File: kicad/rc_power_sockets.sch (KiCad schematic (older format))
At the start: 23 parts, among them IC1 ATTINY85, J1 PIR, J2 433MHZ, J3 433MHZ, P1 ICSP, P2 POWER_IN, Q1 NMOS, Q2 PMOS, U1 MCP1700T

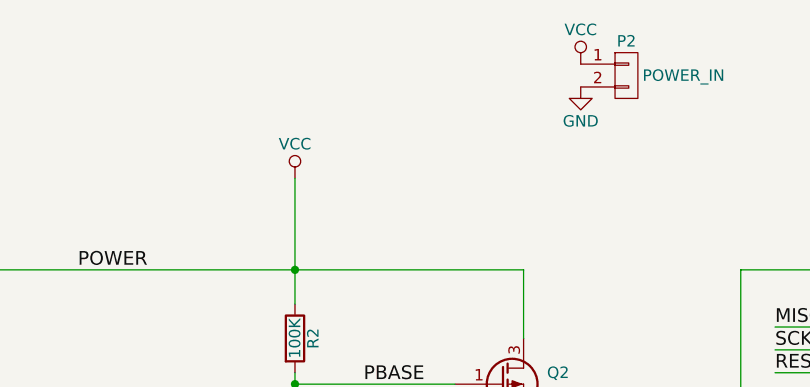
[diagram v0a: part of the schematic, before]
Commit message: Reversed polarity protection
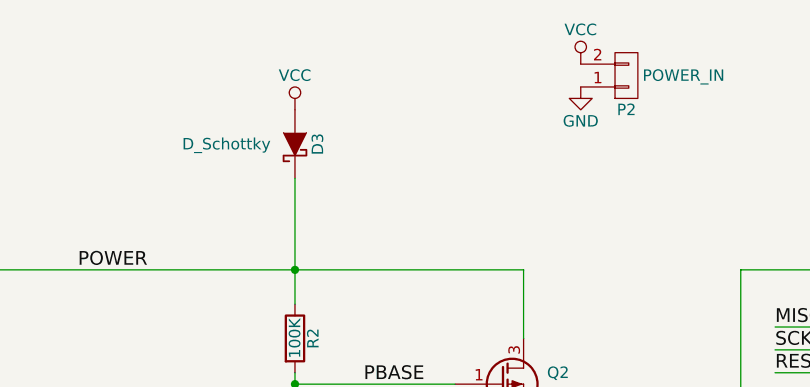
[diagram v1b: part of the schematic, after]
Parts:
- added D3: D_Schottky, Diodes_SMD:SOD-123, symbol D_Schottky
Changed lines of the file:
@@
 L VCC #PWR09
 U 1 1 56E80BFE
-P 5550 1550
-F 0 "#PWR09" H 5550 1400 50  0001 C CNN
-F 1 "VCC" H 5550 1700 50  0000 C CNN
-F 2 "" H 5550 1550 50  0000 C CNN
-F 3 "" H 5550 1550 50  0000 C CNN
-	1    5550 1550
+P 5550 1250
+F 0 "#PWR09" H 5550 1100 50  0001 C CNN
+F 1 "VCC" H 5550 1400 50  0000 C CNN
+F 2 "" H 5550 1250 50  0000 C CNN
+F 3 "" H 5550 1250 50  0000 C CNN
+	1    5550 1250
 	1    0    0    -1
 $EndComp
@@
 F 0 "U1" H 7500 3600 50  0000 C CNN
 F 1 "MCP1700T" H 7350 4100 50  0000 C CNN
-F 2 "TO_SOT_Packages_SMD:SOT-23_Handsoldering" H 7350 4000 50  0000 C CIN
+F 2 "TO_SOT_Packages_SMD:SOT-23_Handsoldering" H 7350 4000 50  0001 C CIN
 F 3 "" H 7350 3900 50  0000 C CNN
 	1    7350 3900
@@
 F 3 "" H 7000 1100 50  0000 C CNN
 	1    7000 1100
-	1    0    0    -1
+	1    0    0    1
 $EndComp
 $Comp
@@
 	0    1    1    0
 $EndComp
+$Comp
+L D_Schottky D3
+U 1 1 56F2954C
+P 5550 1400
+F 0 "D3" H 5550 1300 50  0000 C CNN
+F 1 "D_Schottky" V 5550 1700 50  0000 C CNN
+F 2 "Diodes_SMD:SOD-123" H 5550 1400 50  0001 C CNN
+F 3 "" H 5550 1400 50  0000 C CNN
+	1    5550 1400
+	0    -1   -1   0
+$EndComp
 $EndSCHEMATC

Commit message: Changed voltage regulator cap values
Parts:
- C1, C2: value 10uf -> 1uF
- C3: value 0.1uf -> 0.1uF
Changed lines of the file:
@@
 P 8000 4000
 F 0 "C2" H 8025 4100 50  0000 L CNN
-F 1 "10uf" H 8025 3900 50  0000 L CNN
+F 1 "1uF" H 8025 3900 50  0000 L CNN
 F 2 "Capacitors_SMD:C_0805_HandSoldering" H 8038 3850 50  0001 C CNN
 F 3 "" H 8000 4000 50  0000 C CNN
@@
 P 6700 4000
 F 0 "C1" H 6725 4100 50  0000 L CNN
-F 1 "10uf" H 6725 3900 50  0000 L CNN
+F 1 "1uF" H 6725 3900 50  0000 L CNN
 F 2 "Capacitors_SMD:C_0805_HandSoldering" H 6738 3850 50  0001 C CNN
 F 3 "" H 6700 4000 50  0000 C CNN
@@
 P 8250 5350
 F 0 "C3" H 8275 5450 50  0000 L CNN
-F 1 "0.1uf" H 8275 5250 50  0000 L CNN
+F 1 "0.1uF" H 8275 5250 50  0000 L CNN
 F 2 "Capacitors_SMD:C_0805_HandSoldering" H 8288 5200 50  0001 C CNN
 F 3 "" H 8250 5350 50  0000 C CNN

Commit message: Changed voltage regulator to handle higher input
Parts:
- removed U1: MCP1700T, TO_SOT_Packages_SMD:SOT-23_Handsoldering, symbol APE8865N-12-HF-3
- added U?: NCP4624DSN33T1G, SOT-23-5, symbol TLV70012DDC
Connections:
- wire segments 48 -> 49
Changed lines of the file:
@@
-$EndComp
-$Comp
-L APE8865N-12-HF-3 U1
-U 1 1 56E81B2E
-P 7350 3900
-F 0 "U1" H 7500 3600 50  0000 C CNN
-F 1 "MCP1700T" H 7350 4100 50  0000 C CNN
-F 2 "TO_SOT_Packages_SMD:SOT-23_Handsoldering" H 7350 4000 50  0001 C CIN
-F 3 "" H 7350 3900 50  0000 C CNN
-	1    7350 3900
-	1    0    0    -1
 $EndComp
 $Comp
@@
 	0    -1   -1   0
 $EndComp
+$Comp
+L TLV70012DDC U?
+U 1 1 56F2FC5E
+P 7350 3900
+F 0 "U?" H 7100 4100 50  0000 C CNN
+F 1 "NCP4624DSN33T1G" H 7350 4100 50  0000 C CNN
+F 2 "SOT-23-5" H 7350 4000 50  0000 C CIN
+F 3 "" H 7350 3900 50  0000 C CNN
+	1    7350 3900
+	1    0    0    -1
+$EndComp
+Wire Wire Line
+	6900 3850 6900 4000
 $EndSCHEMATC

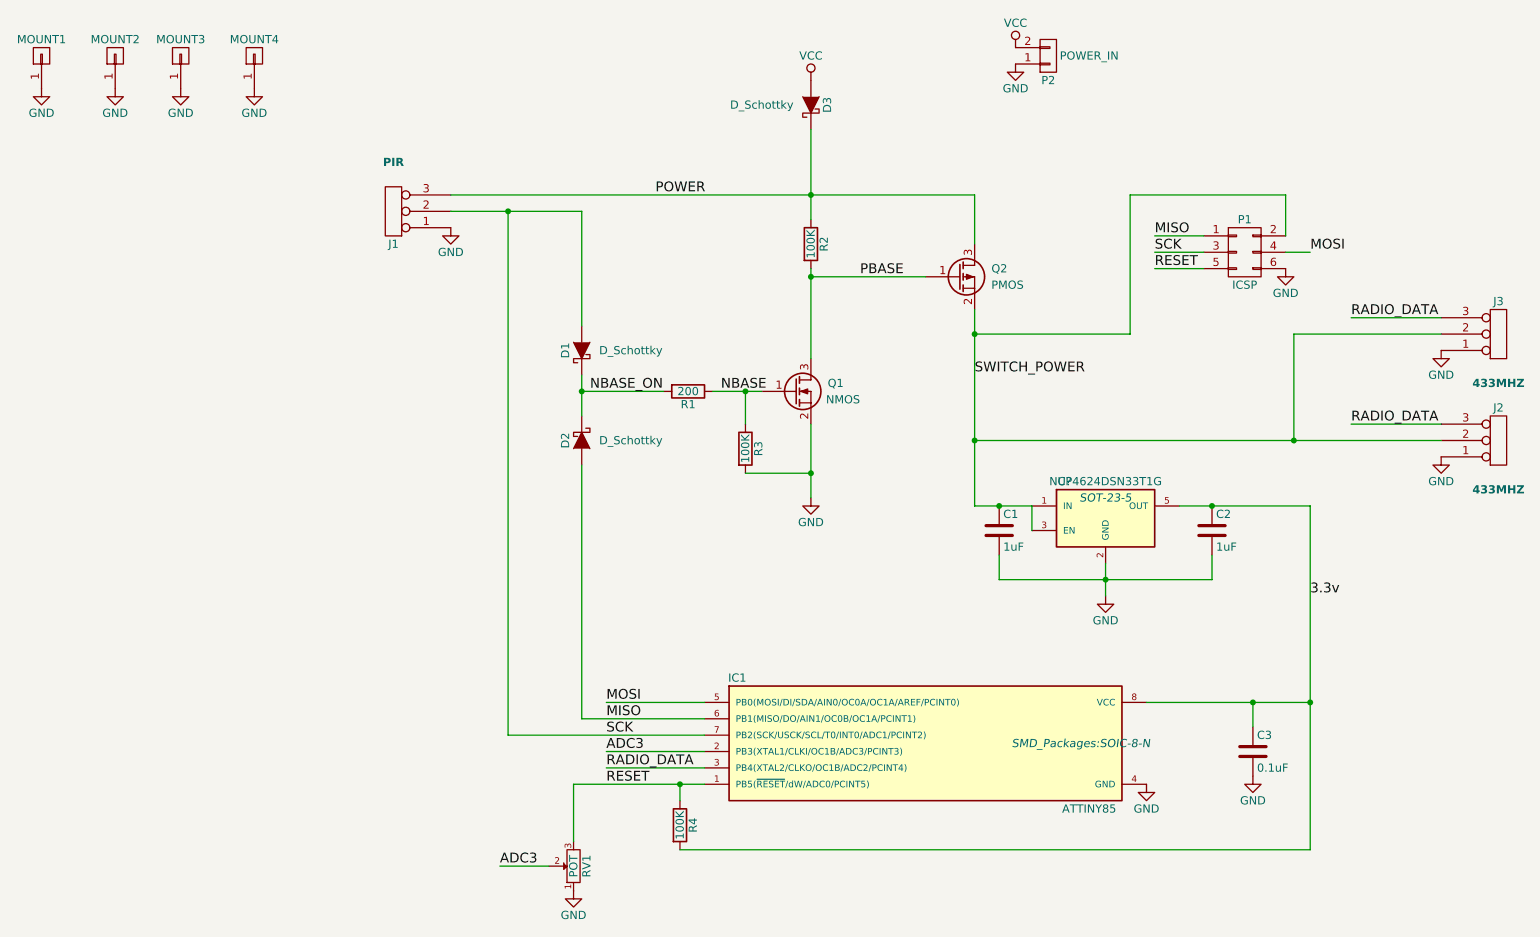
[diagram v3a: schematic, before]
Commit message: Redesign with CR2032
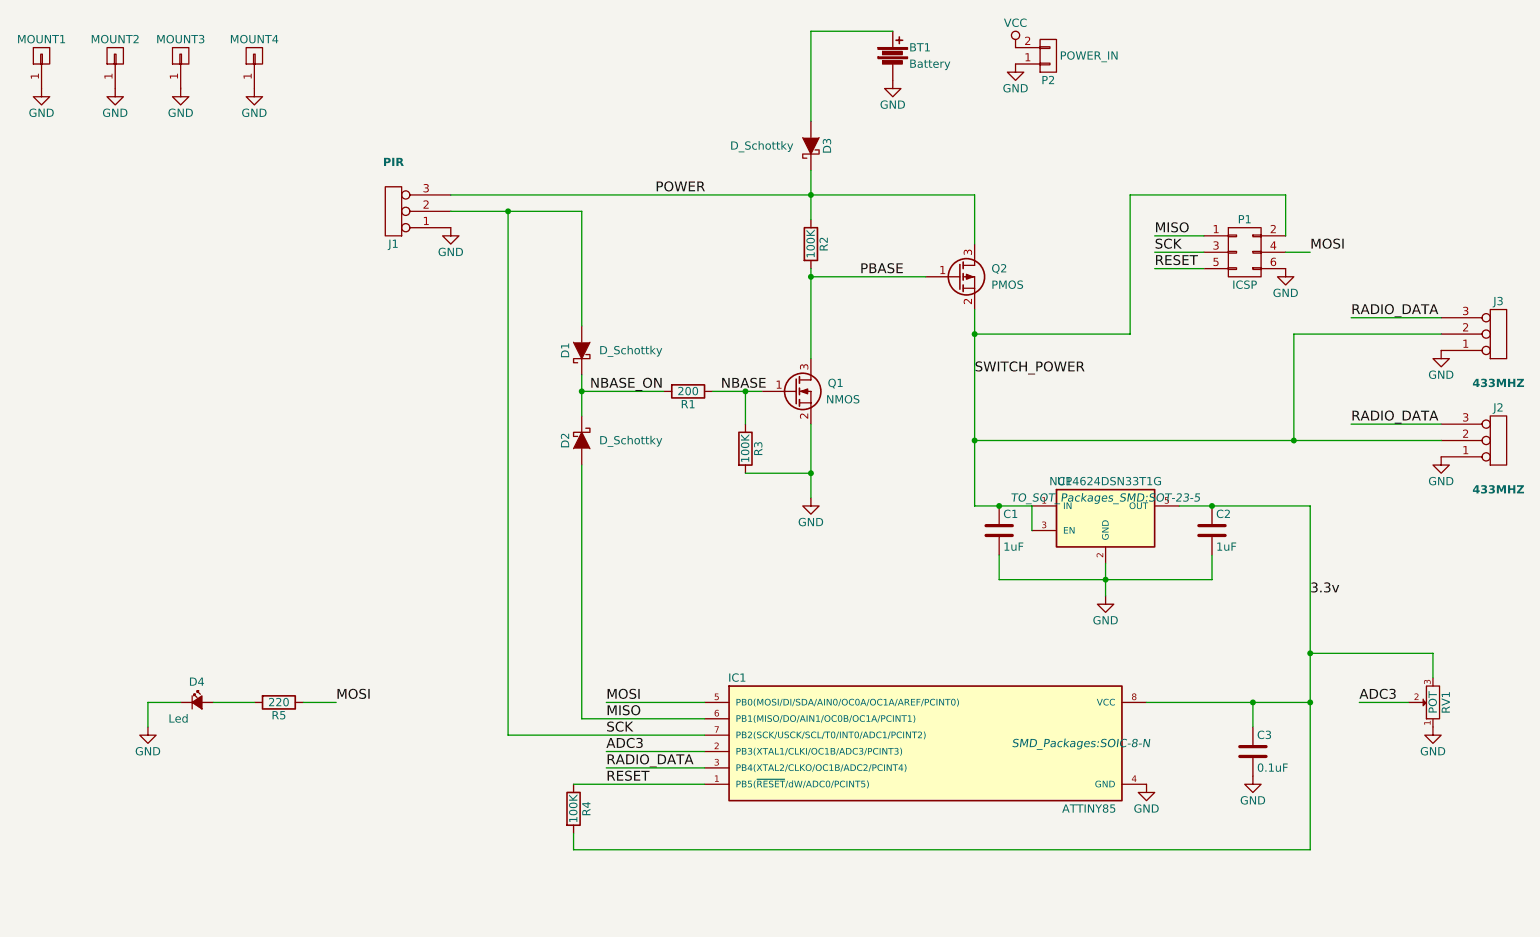
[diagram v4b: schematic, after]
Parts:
- added BT1: Battery, Connect:CR2032H, symbol Battery
- added D4: Led, LEDs:LED_0805, symbol Led_Small
- added R5: 220, Resistors_SMD:R_0805_HandSoldering, symbol R
- U1: renamed from U?; footprint SOT-23-5 -> TO_SOT_Packages_SMD:SOT-23-5
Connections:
- net 3.3v: now also RV1.3
- net GND: now also BT1.2, D4.1 (K)
- net MOSI: now also R5.1
- net RESET: no longer RV1.3
- net VCC: no longer D3.2 (A)
- new net: BT1.1, D3.2 (A)
- new net: D4.2 (A), R5.2
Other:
- moved on the sheet: D3, R4, RV1
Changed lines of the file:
@@
 L R R4
 U 1 1 56D85890
-P 4750 5800
-F 0 "R4" V 4830 5800 50  0000 C CNN
-F 1 "100K" V 4750 5800 50  0000 C CNN
-F 2 "Resistors_SMD:R_0805_HandSoldering" V 4680 5800 50  0001 C CNN
-F 3 "" H 4750 5800 50  0000 C CNN
-	1    4750 5800
+P 4100 5700
+F 0 "R4" V 4180 5700 50  0000 C CNN
+F 1 "100K" V 4100 5700 50  0000 C CNN
+F 2 "Resistors_SMD:R_0805_HandSoldering" V 4030 5700 50  0001 C CNN
+F 3 "" H 4100 5700 50  0000 C CNN
+	1    4100 5700
 	1    0    0    -1
 $EndComp
@@
 L POT-RESCUE-rc_power_sockets RV1
 U 1 1 56E809B9
-P 4100 6050
-F 0 "RV1" H 4100 5970 50  0000 C CNN
-F 1 "POT" H 4100 6050 50  0000 C CNN
-F 2 "Potentiometers:Potentiometer_WirePads_Small" H 4100 6050 50  0001 C CNN
-F 3 "" H 4100 6050 50  0000 C CNN
-	1    4100 6050
+P 9350 5050
+F 0 "RV1" H 9350 4970 50  0000 C CNN
+F 1 "POT" H 9350 5050 50  0000 C CNN
+F 2 "Potentiometers:Potentiometer_WirePads_Small" H 9350 5050 50  0001 C CNN
+F 3 "" H 9350 5050 50  0000 C CNN
+	1    9350 5050
 	0    -1   -1   0
 $EndComp
@@
 L GND #PWR08
 U 1 1 56E80AFC
-P 4100 6200
-F 0 "#PWR08" H 4100 5950 50  0001 C CNN
-F 1 "GND" H 4100 6050 50  0000 C CNN
-F 2 "" H 4100 6200 50  0000 C CNN
-F 3 "" H 4100 6200 50  0000 C CNN
-	1    4100 6200
-	1    0    0    -1
-$EndComp
-$Comp
-L VCC #PWR09
-U 1 1 56E80BFE
-P 5550 1250
-F 0 "#PWR09" H 5550 1100 50  0001 C CNN
-F 1 "VCC" H 5550 1400 50  0000 C CNN
-F 2 "" H 5550 1250 50  0000 C CNN
-F 3 "" H 5550 1250 50  0000 C CNN
-	1    5550 1250
+P 9350 5200
+F 0 "#PWR08" H 9350 4950 50  0001 C CNN
+F 1 "GND" H 9350 5050 50  0000 C CNN
+F 2 "" H 9350 5200 50  0000 C CNN
+F 3 "" H 9350 5200 50  0000 C CNN
+	1    9350 5200
 	1    0    0    -1
 $EndComp
 Text Label 4300 5350 0    60   ~ 0
 ADC3
-Text Label 3650 6050 0    60   ~ 0
+Text Label 8900 5050 0    60   ~ 0
 ADC3
 $Comp
@@
 NBASE
 $Comp
-L GND #PWR010
+L GND #PWR09
 U 1 1 56EEF4F7
 P 6800 1150
-F 0 "#PWR010" H 6800 900 50  0001 C CNN
+F 0 "#PWR09" H 6800 900 50  0001 C CNN
 F 1 "GND" H 6800 1000 50  0000 C CNN
 F 2 "" H 6800 1150 50  0000 C CNN
@@
 RADIO_DATA
 $Comp
-L GND #PWR011
+L GND #PWR010
 U 1 1 56EEFB0C
 P 9400 2900
-F 0 "#PWR011" H 9400 2650 50  0001 C CNN
+F 0 "#PWR010" H 9400 2650 50  0001 C CNN
 F 1 "GND" H 9400 2750 50  0000 C CNN
 F 2 "" H 9400 2900 50  0000 C CNN
@@
 	4900 5050 4300 5050
 Wire Wire Line
-	4100 5550 4900 5550
-Wire Wire Line
 	4900 5450 4300 5450
 Wire Wire Line
@@
 	3700 5250 4900 5250
 Wire Wire Line
-	5550 1550 5550 2100
+	5550 1800 5550 2100
 Wire Wire Line
 	5550 3350 5550 3800
@@
 Connection ~ 5150 3150
 Wire Wire Line
-	4750 5650 4750 5550
-Connection ~ 4750 5550
-Wire Wire Line
-	8600 5950 4750 5950
+	8600 5950 4100 5950
 Connection ~ 8600 5050
 Wire Wire Line
@@
 Connection ~ 8250 5050
 Wire Wire Line
-	3950 6050 3650 6050
+	9200 5050 8900 5050
 Wire Wire Line
 	4900 5350 4300 5350
@@
 Wire Wire Line
 	7600 5050 8600 5050
-Wire Wire Line
-	4100 5550 4100 5900
 Wire Wire Line
 	8450 2200 8450 1950
@@
 $EndComp
 $Comp
-L GND #PWR012
+L GND #PWR011
 U 1 1 56F02CD0
 P 1700 1300
-F 0 "#PWR012" H 1700 1050 50  0001 C CNN
+F 0 "#PWR011" H 1700 1050 50  0001 C CNN
 F 1 "GND" H 1700 1150 50  0000 C CNN
 F 2 "" H 1700 1300 50  0000 C CNN
@@
 $EndComp
 $Comp
-L GND #PWR013
+L GND #PWR012
 U 1 1 56F02EF0
 P 2150 1300
-F 0 "#PWR013" H 2150 1050 50  0001 C CNN
+F 0 "#PWR012" H 2150 1050 50  0001 C CNN
 F 1 "GND" H 2150 1150 50  0000 C CNN
 F 2 "" H 2150 1300 50  0000 C CNN
@@
 $EndComp
 $Comp
-L GND #PWR014
+L GND #PWR013
 U 1 1 56F02F76
 P 850 1300
-F 0 "#PWR014" H 850 1050 50  0001 C CNN
+F 0 "#PWR013" H 850 1050 50  0001 C CNN
 F 1 "GND" H 850 1150 50  0000 C CNN
 F 2 "" H 850 1300 50  0000 C CNN
@@
 $EndComp
 $Comp
-L GND #PWR015
+L GND #PWR014
 U 1 1 56F02F82
 P 1300 1300
-F 0 "#PWR015" H 1300 1050 50  0001 C CNN
+F 0 "#PWR014" H 1300 1050 50  0001 C CNN
 F 1 "GND" H 1300 1150 50  0000 C CNN
 F 2 "" H 1300 1300 50  0000 C CNN
@@
 $EndComp
 $Comp
-L VCC #PWR016
+L VCC #PWR015
 U 1 1 56F0619B
 P 6800 1050
-F 0 "#PWR016" H 6800 900 50  0001 C CNN
+F 0 "#PWR015" H 6800 900 50  0001 C CNN
 F 1 "VCC" H 6800 1200 50  0000 C CNN
 F 2 "" H 6800 1050 50  0000 C CNN
@@
 L D_Schottky D3
 U 1 1 56F2954C
-P 5550 1400
-F 0 "D3" H 5550 1300 50  0000 C CNN
-F 1 "D_Schottky" V 5550 1700 50  0000 C CNN
-F 2 "Diodes_SMD:SOD-123" H 5550 1400 50  0001 C CNN
-F 3 "" H 5550 1400 50  0000 C CNN
-	1    5550 1400
-	0    -1   -1   0
-$EndComp
-$Comp
-L TLV70012DDC U?
+P 5550 1650
+F 0 "D3" H 5550 1550 50  0000 C CNN
+F 1 "D_Schottky" V 5550 1950 50  0000 C CNN
+F 2 "Diodes_SMD:SOD-123" H 5550 1650 50  0001 C CNN
+F 3 "" H 5550 1650 50  0000 C CNN
+	1    5550 1650
+	0    -1   -1   0
+$EndComp
+$Comp
+L TLV70012DDC U1
 U 1 1 56F2FC5E
 P 7350 3900
-F 0 "U?" H 7100 4100 50  0000 C CNN
+F 0 "U1" H 7100 4100 50  0000 C CNN
 F 1 "NCP4624DSN33T1G" H 7350 4100 50  0000 C CNN
-F 2 "SOT-23-5" H 7350 4000 50  0000 C CIN
+F 2 "TO_SOT_Packages_SMD:SOT-23-5" H 7350 4000 50  0000 C CIN
 F 3 "" H 7350 3900 50  0000 C CNN
 	1    7350 3900
@@
 Wire Wire Line
 	6900 3850 6900 4000
+Wire Wire Line
+	4100 5550 4900 5550
+Wire Wire Line
+	4100 5950 4100 5850
+Wire Wire Line
+	9350 4900 9350 4750
+Wire Wire Line
+	9350 4750 8600 4750
+Connection ~ 8600 4750
+$Comp
+L Battery BT1
+U 1 1 56F5C9AA
+P 6050 1100
+F 0 "BT1" H 6150 1150 50  0000 L CNN
+F 1 "Battery" H 6150 1050 50  0000 L CNN
+F 2 "Connect:CR2032H" V 6050 1140 50  0001 C CNN
+F 3 "" V 6050 1140 50  0000 C CNN
+	1    6050 1100
+	1    0    0    -1
+$EndComp
+Wire Wire Line
+	6050 950  5550 950
+Wire Wire Line
+	5550 950  5550 1500
+$Comp
+L GND #PWR016
+U 1 1 56F5CBEA
+P 6050 1250
+F 0 "#PWR016" H 6050 1000 50  0001 C CNN
+F 1 "GND" H 6050 1100 50  0000 C CNN
+F 2 "" H 6050 1250 50  0000 C CNN
+F 3 "" H 6050 1250 50  0000 C CNN
+	1    6050 1250
+	1    0    0    -1
+$EndComp
+$Comp
+L R R5
+U 1 1 56F5D3CF
+P 2300 5050
+F 0 "R5" V 2380 5050 50  0000 C CNN
+F 1 "220" V 2300 5050 50  0000 C CNN
+F 2 "Resistors_SMD:R_0805_HandSoldering" V 2230 5050 50  0001 C CNN
+F 3 "" H 2300 5050 50  0000 C CNN
+	1    2300 5050
+	0    1    1    0
+$EndComp
+$Comp
+L Led_Small D4
+U 1 1 56F5D6D0
+P 1800 5050
+F 0 "D4" H 1750 5175 50  0000 L CNN
+F 1 "Led" H 1625 4950 50  0000 L CNN
+F 2 "LEDs:LED_0805" V 1800 5050 50  0001 C CNN
+F 3 "" V 1800 5050 50  0000 C CNN
+	1    1800 5050
+	1    0    0    -1
+$EndComp
+Text Label 2650 5050 0    60   ~ 0
+MOSI
+Wire Wire Line
+	2450 5050 2650 5050
+Wire Wire Line
+	2150 5050 1900 5050
+$Comp
+L GND #PWR017
+U 1 1 56F5DB12
+P 1500 5200
+F 0 "#PWR017" H 1500 4950 50  0001 C CNN
+F 1 "GND" H 1500 5050 50  0000 C CNN
+F 2 "" H 1500 5200 50  0000 C CNN
+F 3 "" H 1500 5200 50  0000 C CNN
+	1    1500 5200
+	1    0    0    -1
+$EndComp
+Wire Wire Line
+	1700 5050 1500 5050
+Wire Wire Line
+	1500 5050 1500 5200
 $EndSCHEMATC

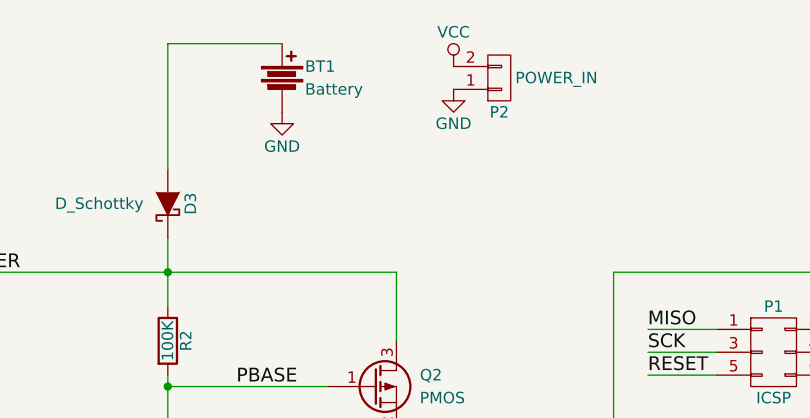
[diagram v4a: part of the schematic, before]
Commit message: Two cell batteries for 6V
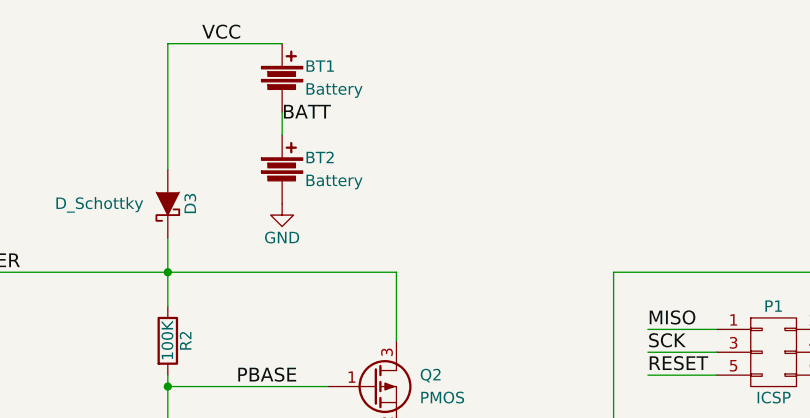
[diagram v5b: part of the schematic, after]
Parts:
- removed P2: POWER_IN, Pin_Headers:Pin_Header_Straight_1x02, symbol CONN_01X02
- added BT2: Battery, Connect:CR2032H, symbol Battery
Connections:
- net GND: now also BT2.2; no longer BT1.2
- net VCC: now also BT1.1, D3.2 (A)
- new net BATT: BT1.2, BT2.1
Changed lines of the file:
@@
 NBASE
-$Comp
-L GND #PWR09
-U 1 1 56EEF4F7
-P 6800 1150
-F 0 "#PWR09" H 6800 900 50  0001 C CNN
-F 1 "GND" H 6800 1000 50  0000 C CNN
-F 2 "" H 6800 1150 50  0000 C CNN
-F 3 "" H 6800 1150 50  0000 C CNN
-	1    6800 1150
-	1    0    0    -1
-$EndComp
 $Comp
 L SIL3 J3
@@
 RADIO_DATA
 $Comp
-L GND #PWR010
+L GND #PWR09
 U 1 1 56EEFB0C
 P 9400 2900
-F 0 "#PWR010" H 9400 2650 50  0001 C CNN
+F 0 "#PWR09" H 9400 2650 50  0001 C CNN
 F 1 "GND" H 9400 2750 50  0000 C CNN
 F 2 "" H 9400 2900 50  0000 C CNN
@@
 $EndComp
 $Comp
-L GND #PWR011
+L GND #PWR010
 U 1 1 56F02CD0
 P 1700 1300
-F 0 "#PWR011" H 1700 1050 50  0001 C CNN
+F 0 "#PWR010" H 1700 1050 50  0001 C CNN
 F 1 "GND" H 1700 1150 50  0000 C CNN
 F 2 "" H 1700 1300 50  0000 C CNN
@@
 $EndComp
 $Comp
-L GND #PWR012
+L GND #PWR011
 U 1 1 56F02EF0
 P 2150 1300
-F 0 "#PWR012" H 2150 1050 50  0001 C CNN
+F 0 "#PWR011" H 2150 1050 50  0001 C CNN
 F 1 "GND" H 2150 1150 50  0000 C CNN
 F 2 "" H 2150 1300 50  0000 C CNN
@@
 $EndComp
 $Comp
-L GND #PWR013
+L GND #PWR012
 U 1 1 56F02F76
 P 850 1300
-F 0 "#PWR013" H 850 1050 50  0001 C CNN
+F 0 "#PWR012" H 850 1050 50  0001 C CNN
 F 1 "GND" H 850 1150 50  0000 C CNN
 F 2 "" H 850 1300 50  0000 C CNN
@@
 $EndComp
 $Comp
-L GND #PWR014
+L GND #PWR013
 U 1 1 56F02F82
 P 1300 1300
-F 0 "#PWR014" H 1300 1050 50  0001 C CNN
+F 0 "#PWR013" H 1300 1050 50  0001 C CNN
 F 1 "GND" H 1300 1150 50  0000 C CNN
 F 2 "" H 1300 1300 50  0000 C CNN
@@
 	1    1300 1300
 	1    0    0    -1
-$EndComp
-$Comp
-L VCC #PWR015
-U 1 1 56F0619B
-P 6800 1050
-F 0 "#PWR015" H 6800 900 50  0001 C CNN
-F 1 "VCC" H 6800 1200 50  0000 C CNN
-F 2 "" H 6800 1050 50  0000 C CNN
-F 3 "" H 6800 1050 50  0000 C CNN
-	1    6800 1050
-	1    0    0    -1
-$EndComp
-$Comp
-L CONN_01X02 P2
-U 1 1 56F0648D
-P 7000 1100
-F 0 "P2" H 7000 1250 50  0000 C CNN
-F 1 "POWER_IN" H 7250 1100 50  0000 C CNN
-F 2 "Pin_Headers:Pin_Header_Straight_1x02" H 7000 1100 50  0001 C CNN
-F 3 "" H 7000 1100 50  0000 C CNN
-	1    7000 1100
-	1    0    0    1
 $EndComp
 $Comp
@@
 	5550 950  5550 1500
 $Comp
-L GND #PWR016
+L GND #PWR014
 U 1 1 56F5CBEA
-P 6050 1250
-F 0 "#PWR016" H 6050 1000 50  0001 C CNN
-F 1 "GND" H 6050 1100 50  0000 C CNN
-F 2 "" H 6050 1250 50  0000 C CNN
-F 3 "" H 6050 1250 50  0000 C CNN
-	1    6050 1250
+P 6050 1650
+F 0 "#PWR014" H 6050 1400 50  0001 C CNN
+F 1 "GND" H 6050 1500 50  0000 C CNN
+F 2 "" H 6050 1650 50  0000 C CNN
+F 3 "" H 6050 1650 50  0000 C CNN
+	1    6050 1650
 	1    0    0    -1
 $EndComp
@@
 	2150 5050 1900 5050
 $Comp
-L GND #PWR017
+L GND #PWR015
 U 1 1 56F5DB12
 P 1500 5200
-F 0 "#PWR017" H 1500 4950 50  0001 C CNN
+F 0 "#PWR015" H 1500 4950 50  0001 C CNN
 F 1 "GND" H 1500 5050 50  0000 C CNN
 F 2 "" H 1500 5200 50  0000 C CNN
@@
 Wire Wire Line
 	1500 5050 1500 5200
+$Comp
+L Battery BT2
+U 1 1 56F65688
+P 6050 1500
+F 0 "BT2" H 6150 1550 50  0000 L CNN
+F 1 "Battery" H 6150 1450 50  0000 L CNN
+F 2 "Connect:CR2032H" V 6050 1540 50  0001 C CNN
+F 3 "" V 6050 1540 50  0000 C CNN
+	1    6050 1500
+	1    0    0    -1
+$EndComp
+Wire Wire Line
+	6050 1250 6050 1350
+Text Label 6050 1300 0    60   ~ 0
+BATT
+Text Label 5700 950  0    60   ~ 0
+VCC
 $EndSCHEMATC
